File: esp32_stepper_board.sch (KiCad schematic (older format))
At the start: 49 parts, among them J1 Serial, J10 Aux2_GPIO, J11 DC_PWR, J12 Micro_SD_Card, J2 Servo, J3 Stepper A/X, J4 Stepper B/Y, J5 Stepper C/Y, J6 Endstop A/X, J7 Endstop B/Y, J8 Endstop C/Z, J9 Aux1_I2C, SW1 SW_Push, SW2 SW_Push, SW3 SW_Push, SW4 Rotary_Encoder_Switch, U1 LM1117-5.0, U2 LM1117-3.3, U3 PCF8574, U4 OLED_I2C, U5 ESP-WROOM-32D, U6 STEPSTICK, U7 STEPSTICK, U8 STEPSTICK

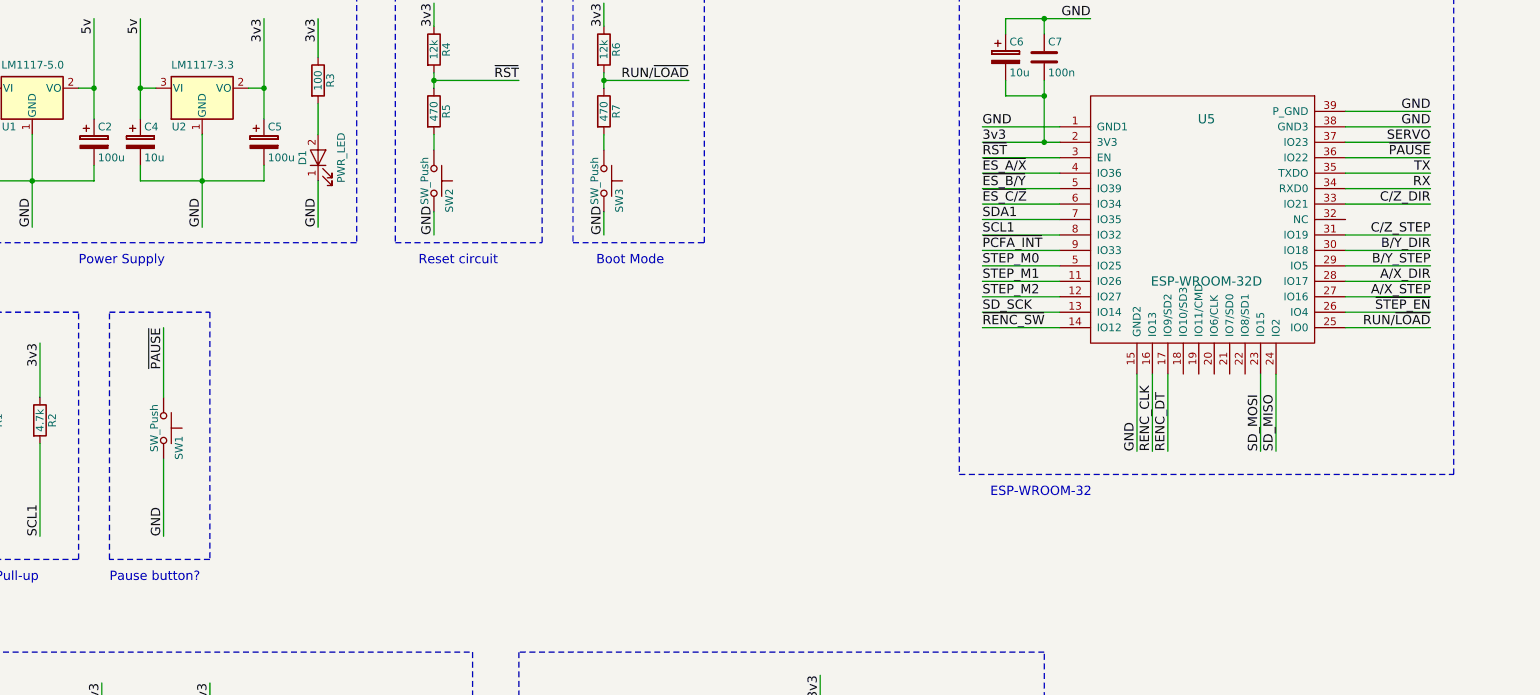
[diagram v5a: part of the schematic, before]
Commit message: Fixed mistake on WROOM symbol & removed pause button
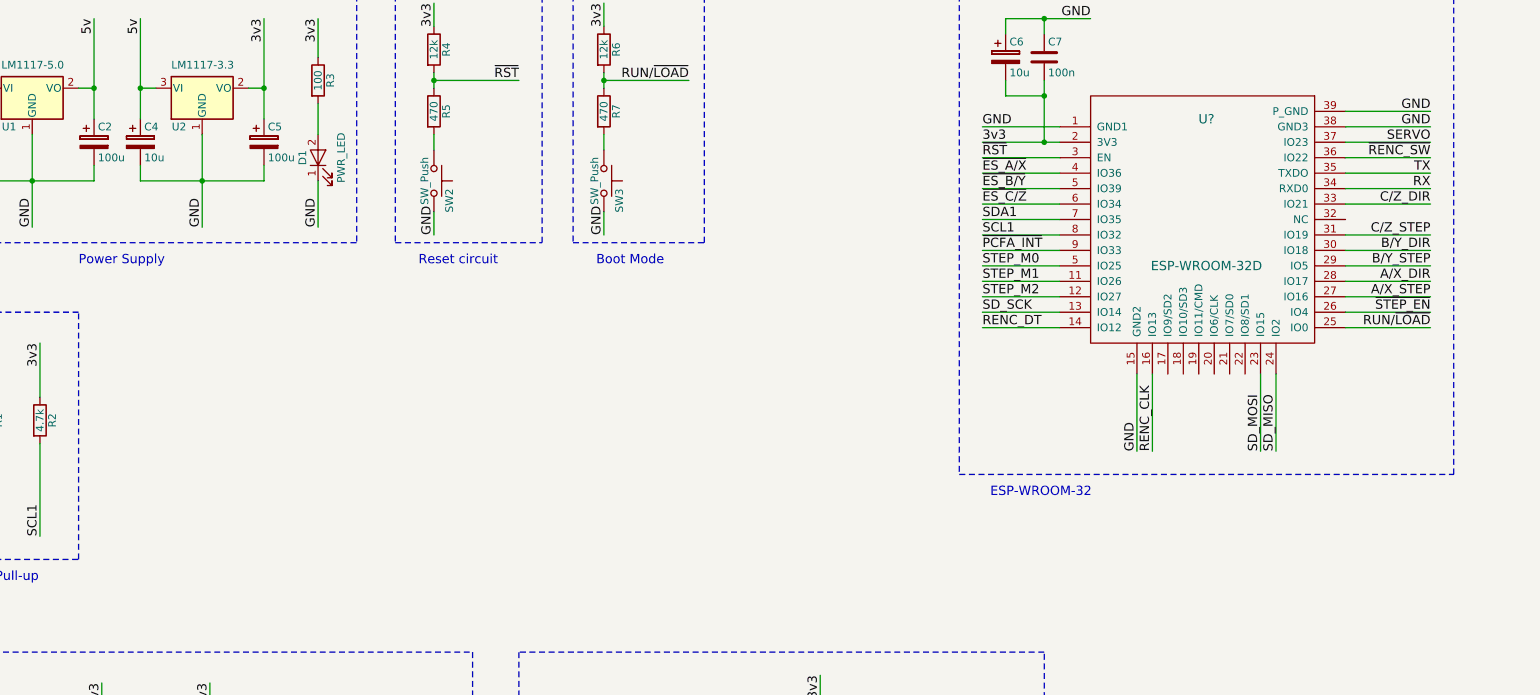
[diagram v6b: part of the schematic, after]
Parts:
- removed SW1: SW_Push, symbol SW_Push
- removed U5: ESP-WROOM-32D, symbol ESP-WROOM-32D
- added U?: ESP-WROOM-32D, symbol ESP-WROOM-32D
- C1, C4, C6: footprint (none) -> Capacitors_SMD:CP_Elec_5x5.3
- C10, C11, C2, C5, C9: footprint (none) -> Capacitors_SMD:CP_Elec_6.3x7.7
- C3, C7, C8: footprint (none) -> Capacitors_SMD:C_0805
- D1: footprint (none) -> LEDs:LED_0805
- J1, J2, J6, J7, J8: footprint (none) -> Connectors_JST:JST_PH_B3B-PH-K_03x2.00mm_Straight
- J10: footprint (none) -> Connectors_JST:JST_PH_B12B-PH-K_12x2.00mm_Straight
- J11: footprint (none) -> Connect:BARREL_JACK
- J12: footprint (none) -> Connect:microSD_Card_Receptacle_Wuerth_693072010801
- J3, J4, J5, J9: footprint (none) -> Connectors_JST:JST_PH_B4B-PH-K_04x2.00mm_Straight
- R1, R10, R11, R12, R13, R2, R3, R4, R5, R6, R7, R8, R9: footprint (none) -> Resistors_SMD:R_0805
- SW2, SW3: footprint (none) -> custom:TactSw
- U1, U2: footprint (none) -> TO_SOT_Packages_SMD:SOT-223
- U3: footprint (none) -> Housings_SOIC:SOIC-16_3.9x9.9mm_Pitch1.27mm
- U6, U7, U8: footprint (none) -> custom:Stepstick
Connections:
- net 3v3: now also U?.2 (3V3)
- net A/X_DIR: now also U?.28 (IO17)
- net A/X_STEP: now also U?.27 (IO16)
- net B/Y_DIR: now also U?.30 (IO18)
- net B/Y_STEP: now also U?.29 (IO5)
- net C/Z_DIR: now also U?.33 (IO21)
- net C/Z_STEP: now also U?.31 (IO19)
- net GND: now also U?.1 (GND1), U?.15 (GND2), U?.38 (GND3), U?.39 (P_GND)
- net RENC_CLK: now also U?.16 (IO13)
- net RENC_DT: now also U?.14 (IO12)
- net RUN/~LOAD: now also U?.25 (IO0)
- net RX: now also U?.34 (RXD0)
- net SCL1: now also U?.8 (IO32)
- net SDA1: now also U?.7 (IO35)
- net SD_MISO: now also U?.24 (IO2)
- net SD_MOSI: now also U?.23 (IO15)
- net SD_SCK: now also U?.13 (IO14)
- net SERVO: now also U?.37 (IO23)
- net STEP_M0: now also U?.5 (IO39)
- net STEP_M1: now also U?.11 (IO26)
- net STEP_M2: now also U?.12 (IO27)
- net TX: now also U?.35 (TXDO)
- net ~ES_A/X: now also U?.4 (IO36)
- net ~ES_B/Y: now also U?.5 (IO39)
- net ~ES_C/Z: now also U?.6 (IO34)
- net ~PCFA_INT: now also U?.9 (IO33)
- net ~RENC_SW: now also U?.36 (IO22)
- net ~RST: now also U?.3 (EN)
- net ~STEP_EN: now also U?.26 (IO4)
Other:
- note removed: "Pause button?"

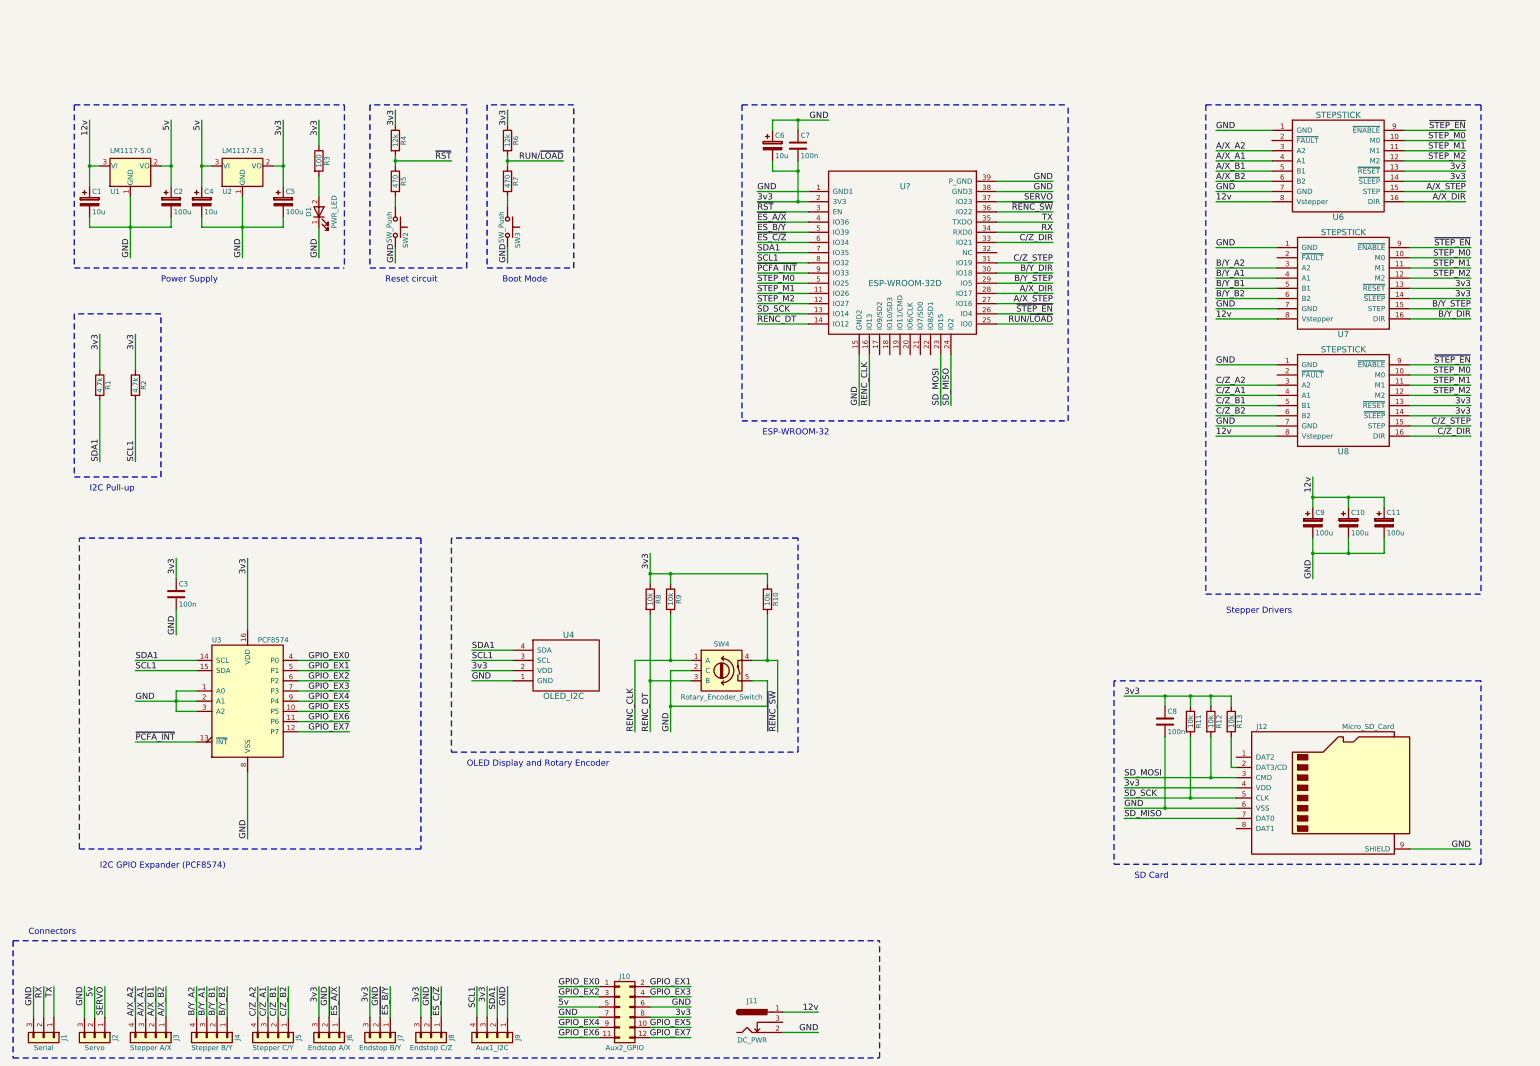
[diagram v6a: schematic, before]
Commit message: Schematic using Devkitc
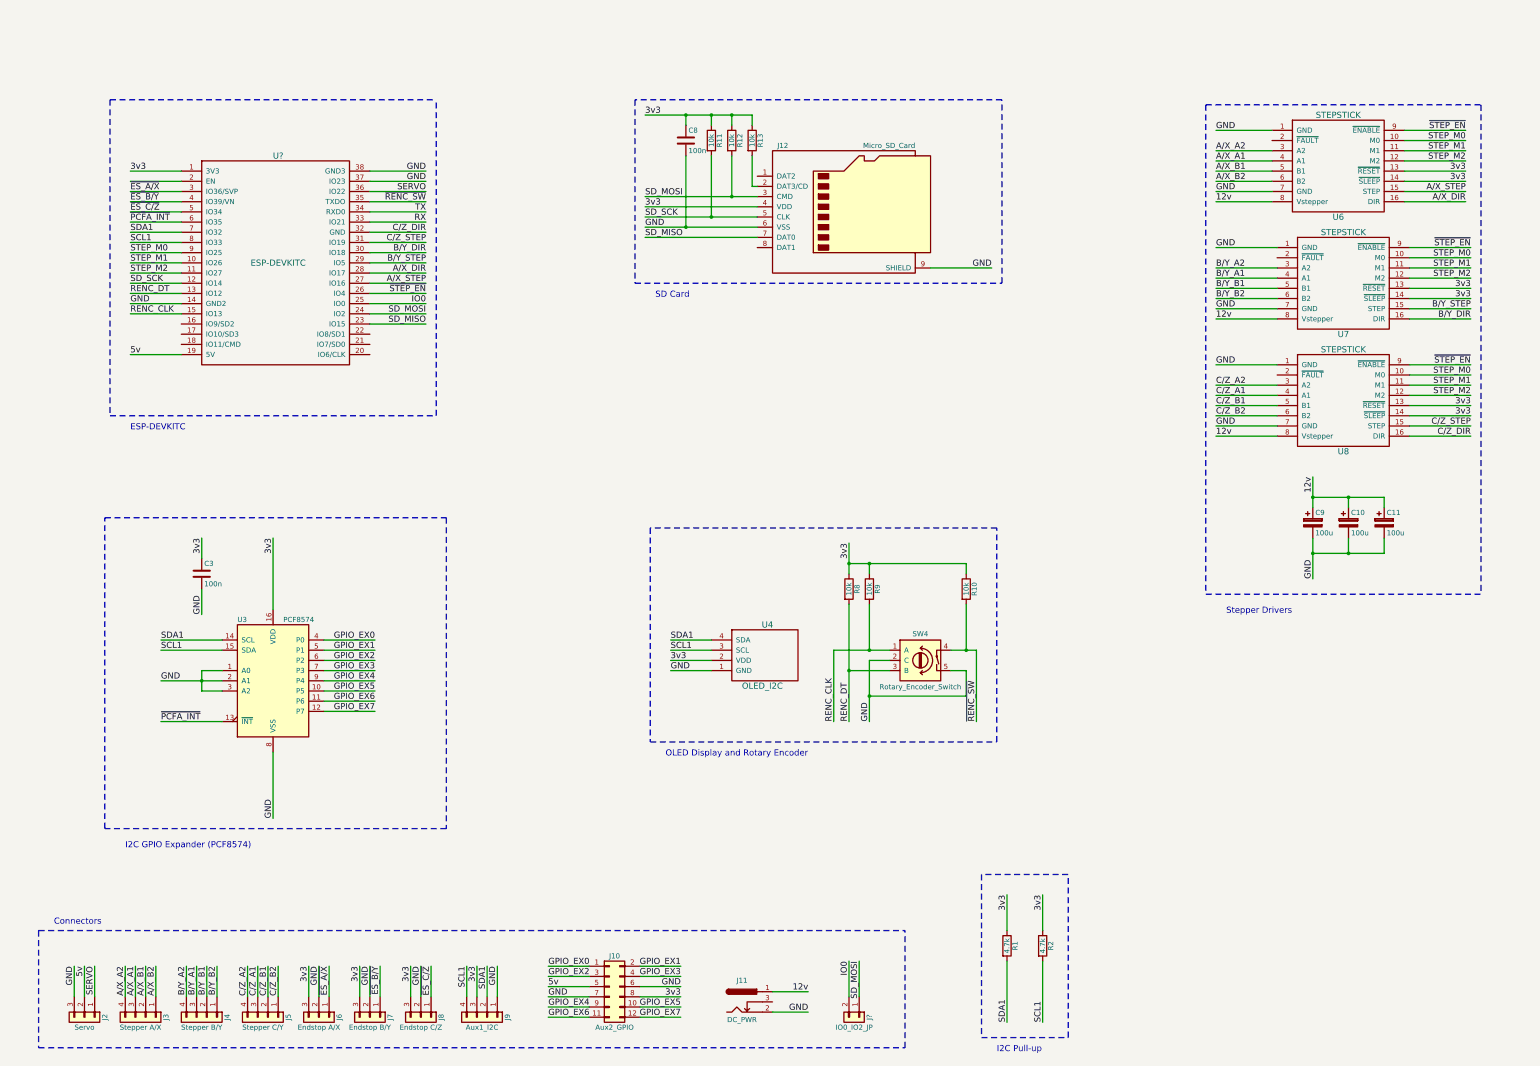
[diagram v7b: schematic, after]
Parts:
- removed C1, C4, C6: 10u, Capacitors_SMD:CP_Elec_5x5.3, symbol CP
- removed C2, C5: 100u, Capacitors_SMD:CP_Elec_6.3x7.7, symbol CP
- removed C7: 100n, Capacitors_SMD:C_0805, symbol C
- removed D1: PWR_LED, LEDs:LED_0805, symbol LED
- removed J1: Serial, Connectors_JST:JST_PH_B3B-PH-K_03x2.00mm_Straight, symbol Conn_01x03
- removed R3: 100, Resistors_SMD:R_0805, symbol R
- removed R4, R6: 12k, Resistors_SMD:R_0805, symbol R
- removed R5, R7: 470, Resistors_SMD:R_0805, symbol R
- removed SW2, SW3: SW_Push, custom:TactSw, symbol SW_Push
- removed U1: LM1117-5.0, TO_SOT_Packages_SMD:SOT-223, symbol LM1117-5.0
- removed U2: LM1117-3.3, TO_SOT_Packages_SMD:SOT-223, symbol LM1117-3.3
- removed U?: ESP-WROOM-32D, symbol ESP-WROOM-32D
- added J?: IO0_IO2_JP, symbol Conn_01x02
- added U?: ESP-DEVKITC, symbol ESP-DEVKITC
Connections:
- net 3v3: now also U?.1 (3V3)
- net 5v: now also U?.19 (5V)
- net A/X_DIR: now also U?.28 (IO17)
- net A/X_STEP: now also U?.27 (IO16)
- net B/Y_DIR: now also U?.30 (IO18)
- net B/Y_STEP: now also U?.29 (IO5)
- net C/Z_DIR: now also U?.32 (GND)
- net C/Z_STEP: now also U?.31 (IO19)
- net GND: now also U?.14 (GND2), U?.37 (IO23), U?.38 (GND3)
- net RENC_CLK: now also U?.15 (IO13)
- net RENC_DT: now also U?.13 (IO12)
- net RX: now also U?.33 (IO21)
- net SCL1: now also U?.8 (IO33)
- net SDA1: now also U?.7 (IO32)
- net SD_MISO: now also U?.23 (IO15)
- net SD_MOSI: now also J?.1 (Pin_1), U?.24 (IO2)
- net SD_SCK: now also U?.12 (IO14)
- net SERVO: now also U?.36 (IO22)
- net STEP_M0: now also U?.9 (IO25)
- net STEP_M1: now also U?.10 (IO26)
- net STEP_M2: now also U?.11 (IO27)
- net TX: now also U?.34 (RXD0)
- net ~ES_A/X: now also U?.3 (IO36/SVP)
- net ~ES_B/Y: now also U?.4 (IO39/VN)
- net ~ES_C/Z: now also U?.5 (IO34)
- net ~PCFA_INT: now also U?.6 (IO35)
- net ~RENC_SW: now also U?.35 (TXDO)
- net ~STEP_EN: now also U?.26 (IO4)
- new net IO0: J?.2 (Pin_2), U?.25 (IO0)
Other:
- note added: "ESP-DEVKITC"
- note removed: "Boot Mode"
- note removed: "ESP-WROOM-32"
- note removed: "Power Supply"
- note removed: "Reset circuit"
- moved on the sheet: C3, C8, J10, J11, J12, J2, J3, J4, J5, J6, J7, J8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

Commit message: Added external power and other changes for devkitc
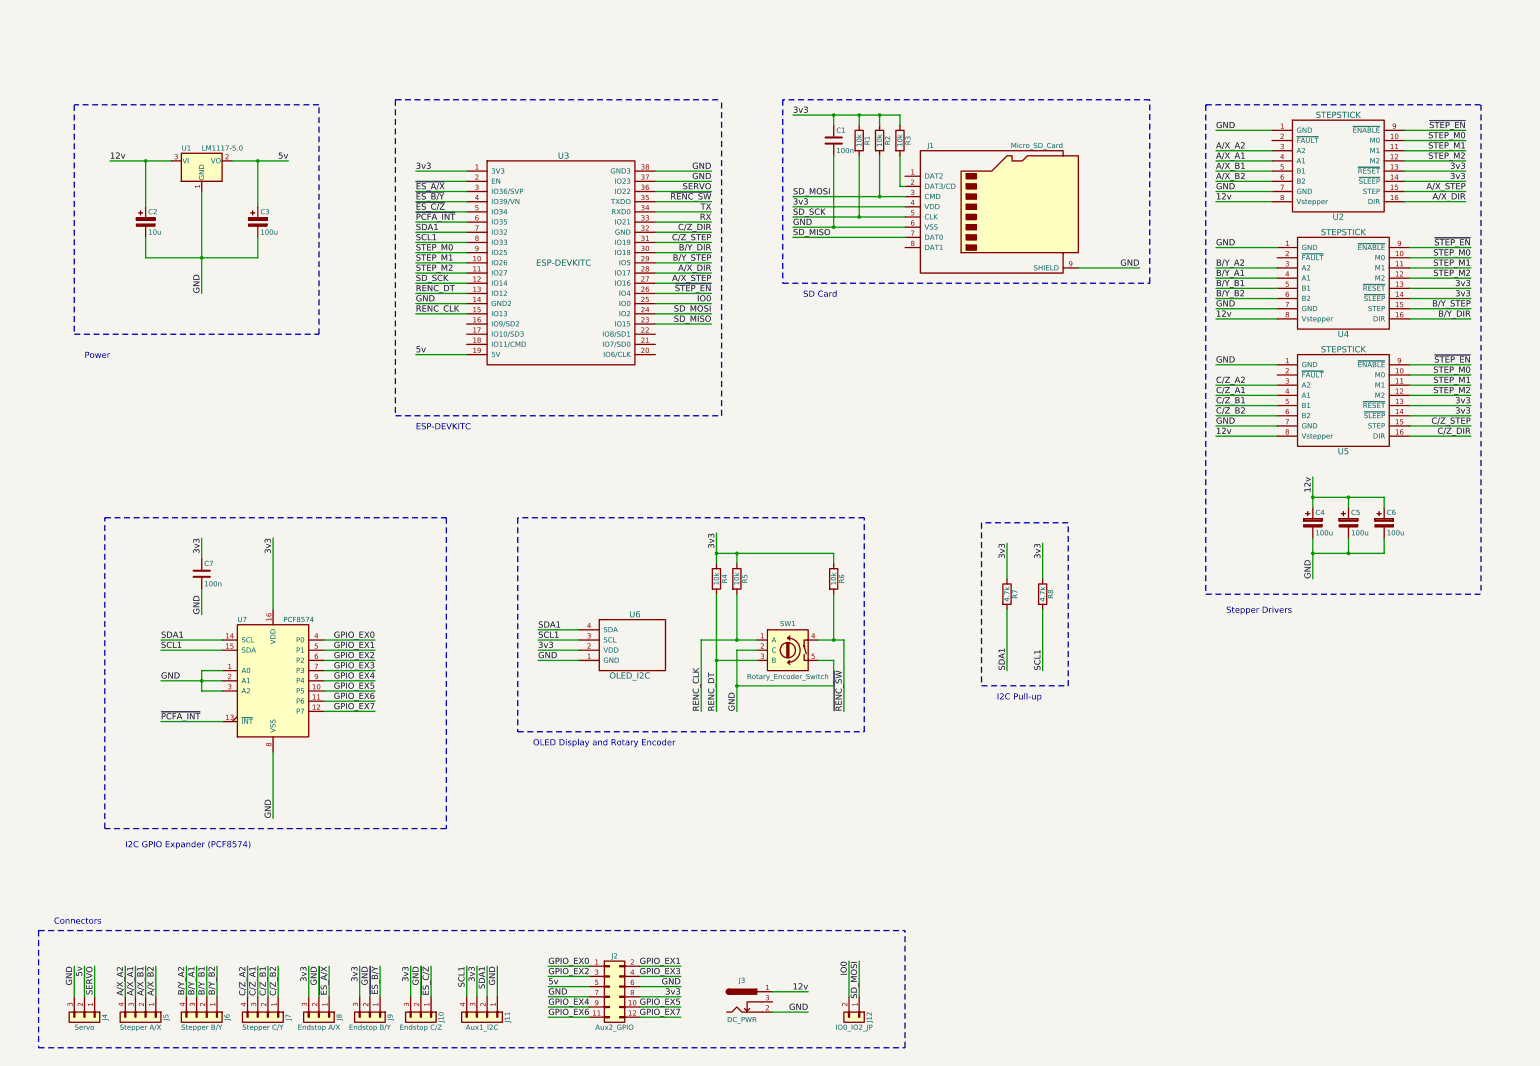
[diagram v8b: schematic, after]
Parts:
- added C2: 10u, symbol CP
- added C3: 100u, symbol CP
- added U1: LM1117-5.0, symbol LM1117-5.0
- gave numbers to parts that had none: 2
- renumbered C8 to C1, C9 to C4, C10 to C5, C11 to C6, C3 to C7, J12 to J1, J8 to J10, J9 to J11, J10 to J2, J11 to J3, J2 to J4, J3 to J5, J4 to J6, J5 to J7, J6 to J8, J7 to J9, R11 to R1, R12 to R2, R13 to R3, R8 to R4, R9 to R5, R10 to R6, R1 to R7, R2 to R8, SW4 to SW1, U6 to U2, U7 to U4, U8 to U5, U4 to U6, U3 to U7
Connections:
- net 12v: now also C2.1, U1.3 (VI)
- net 5v: now also C3.1, U1.2 (VO)
- net GND: now also C2.2, C3.2, U1.1 (GND)
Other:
- note added: "Power"
- moved on the sheet: C1, J1, R1, R2, R3, R4, R5, R6, R7, R8, SW1, U3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
